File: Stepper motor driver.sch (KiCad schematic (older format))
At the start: 16 parts, among them P1 CONN_01X04, P2 CONN_01X06, Q1 TIP120, Q2 TIP120, Q3 TIP120, Q4 TIP120, U1 74LS175, U2 74LS157

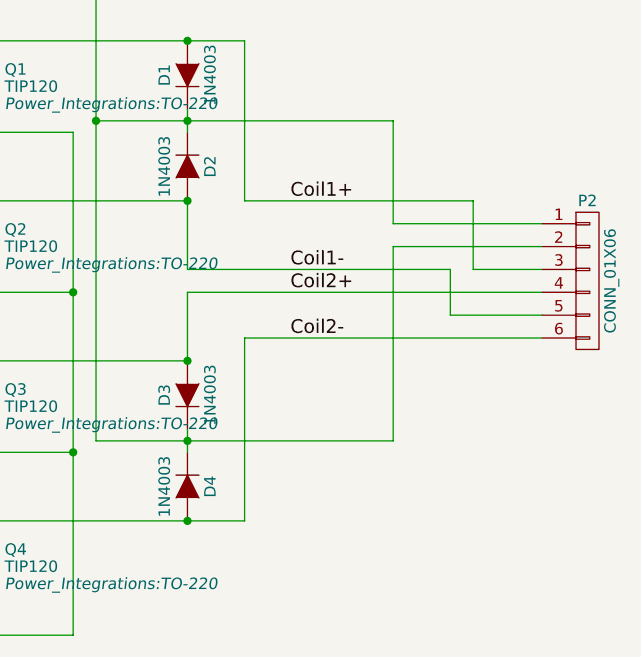
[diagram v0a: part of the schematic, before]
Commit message: Completed initial routing
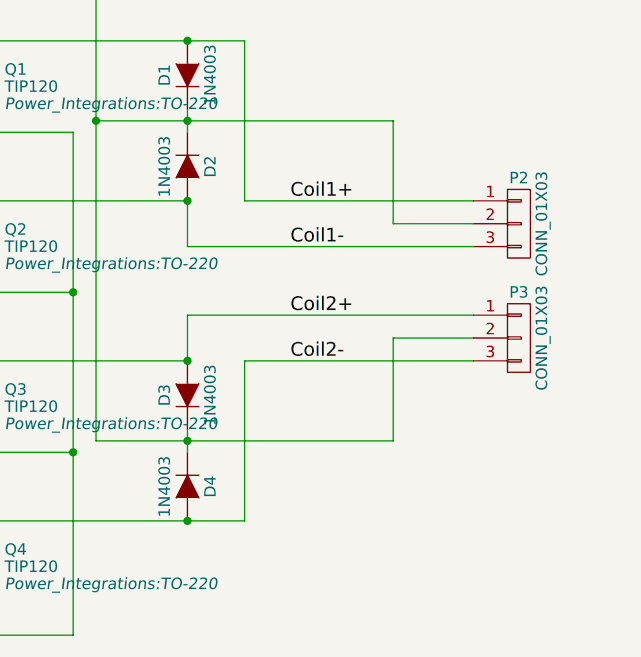
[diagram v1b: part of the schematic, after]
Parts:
- removed P2: CONN_01X06, Connectors_Molex:Molex_KK-6410-06_06x2.54mm_Straight, symbol CONN_01X06
- added P2, P3: CONN_01X03, Pin_Headers:Pin_Header_Straight_1x03_Pitch1.27mm, symbol CONN_01X03
- P1: footprint Connectors_Molex:Molex_KK-6410-04_04x2.54mm_Straight -> Pin_Headers:Pin_Header_Straight_1x04_Pitch1.27mm
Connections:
- net Coil1+: now also P2.1 (P1)
- net Coil1-: now also P2.3 (P3)
- net Coil2+: now also P3.1 (P1)
- net Coil2-: now also P3.3 (P3)
- net VCC: now also P2.2 (P2), P3.2 (P2)
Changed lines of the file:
@@
 Text Label 9650 3900 0    60   ~ 0
 Coil1+
-Text Label 9650 4200 0    60   ~ 0
+Text Label 9650 4100 0    60   ~ 0
 Coil1-
-Text Label 9650 4300 0    60   ~ 0
+Text Label 9650 4400 0    60   ~ 0
 Coil2+
-Text Label 9650 4500 0    60   ~ 0
+Text Label 9650 4600 0    60   ~ 0
 Coil2-
 $Comp
-L CONN_01X06 P2
-U 1 1 58B0F217
-P 10950 4250
-F 0 "P2" H 10950 4600 50  0000 C CNN
-F 1 "CONN_01X06" V 11050 4250 50  0000 C CNN
-F 2 "Connectors_Molex:Molex_KK-6410-06_06x2.54mm_Straight" H 10950 4250 50  0001 C CNN
-F 3 "" H 10950 4250 50  0000 C CNN
-	1    10950 4250
+L CONN_01X04 P1
+U 1 1 58AC3CBE
+P 1500 3450
+F 0 "P1" H 1500 3700 50  0000 C CNN
+F 1 "CONN_01X04" V 1600 3450 50  0000 C CNN
+F 2 "Pin_Headers:Pin_Header_Straight_1x04_Pitch1.27mm" H 1500 3450 50  0001 C CNN
+F 3 "" H 1500 3450 50  0000 C CNN
+	1    1500 3450
+	-1   0    0    1
+$EndComp
+$Comp
+L CONN_01X03 P3
+U 1 1 58B39702
+P 10650 4500
+F 0 "P3" H 10650 4700 50  0000 C CNN
+F 1 "CONN_01X03" V 10750 4500 50  0000 C CNN
+F 2 "Pin_Headers:Pin_Header_Straight_1x03_Pitch1.27mm" H 10650 4500 50  0001 C CNN
+F 3 "" H 10650 4500 50  0000 C CNN
+	1    10650 4500
+	1    0    0    -1
+$EndComp
+$Comp
+L CONN_01X03 P2
+U 1 1 58B396A2
+P 10650 4000
+F 0 "P2" H 10650 4200 50  0000 C CNN
+F 1 "CONN_01X03" V 10750 4000 50  0000 C CNN
+F 2 "Pin_Headers:Pin_Header_Straight_1x03_Pitch1.27mm" H 10650 4000 50  0001 C CNN
+F 3 "" H 10650 4000 50  0000 C CNN
+	1    10650 4000
 	1    0    0    -1
 $EndComp
@@
 	8800 3550 10100 3550
 Wire Wire Line
-	8800 4950 10100 4950
-Wire Wire Line
 	8700 5800 8700 3600
 Wire Wire Line
@@
 	8250 3900 9200 3900
 Wire Wire Line
-	9200 3900 9200 4200
-Wire Wire Line
-	9200 4200 10350 4200
-Wire Wire Line
-	8250 5300 9450 5300
-Wire Wire Line
-	9200 4300 10750 4300
-Wire Wire Line
-	9200 4300 9200 4600
-Wire Wire Line
 	9200 4600 8250 4600
 Wire Wire Line
@@
 	4250 3850 5250 3850
 Wire Wire Line
-	9450 5300 9450 4500
-Wire Wire Line
-	9450 4500 10750 4500
-Wire Wire Line
-	10100 4950 10100 4100
-Wire Wire Line
-	10450 4200 10750 4200
-Wire Wire Line
 	10100 3550 10100 4000
 Wire Wire Line
-	10100 4000 10750 4000
-Wire Wire Line
-	10100 4100 10750 4100
-Wire Wire Line
 	9450 3200 9450 3900
 Wire Wire Line
 	9450 3900 10450 3900
-Wire Wire Line
-	10450 3900 10450 4200
-Wire Wire Line
-	10350 4200 10350 4400
-Wire Wire Line
-	10350 4400 10750 4400
 Connection ~ 2350 3600
 Wire Wire Line
 	2550 3500 2550 4150
-$Comp
-L CONN_01X04 P1
-U 1 1 58AC3CBE
-P 1500 3450
-F 0 "P1" H 1500 3700 50  0000 C CNN
-F 1 "CONN_01X04" V 1600 3450 50  0000 C CNN
-F 2 "Connectors_Molex:Molex_KK-6410-04_04x2.54mm_Straight" H 1500 3450 50  0001 C CNN
-F 3 "" H 1500 3450 50  0000 C CNN
-	1    1500 3450
-	-1   0    0    1
-$EndComp
 Wire Wire Line
 	2350 3600 1700 3600
@@
 Wire Wire Line
 	1700 3300 2250 3300
+Wire Wire Line
+	10100 4000 10450 4000
+Wire Wire Line
+	9200 3900 9200 4100
+Wire Wire Line
+	9200 4100 10450 4100
+Wire Wire Line
+	9200 4400 10450 4400
+Wire Wire Line
+	9200 4600 9200 4400
+Wire Wire Line
+	8800 4950 10100 4950
+Wire Wire Line
+	9450 5300 9450 4600
+Wire Wire Line
+	9450 4600 10450 4600
+Wire Wire Line
+	8250 5300 9450 5300
+Wire Wire Line
+	10100 4950 10100 4500
+Wire Wire Line
+	10100 4500 10450 4500
 $EndSCHEMATC
